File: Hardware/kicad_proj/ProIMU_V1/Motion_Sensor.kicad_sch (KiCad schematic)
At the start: 18 parts, among them U1 BMP280, U2 BNO055, Y1 Crystal

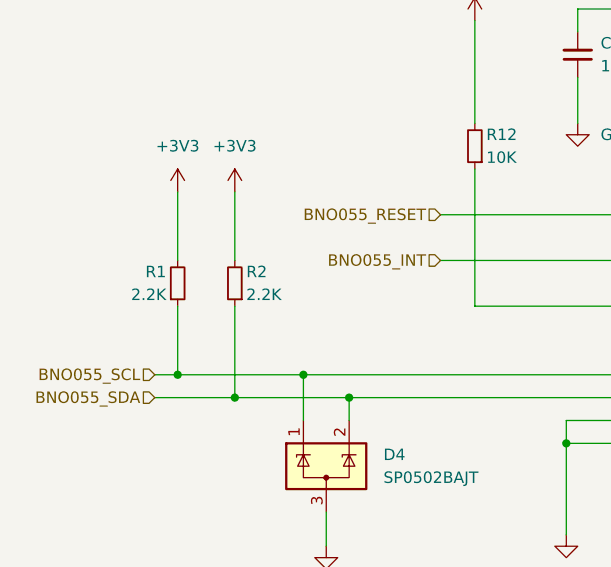
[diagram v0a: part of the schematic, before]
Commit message: Added New USB footprint. This will be used through entire project and will not be changed
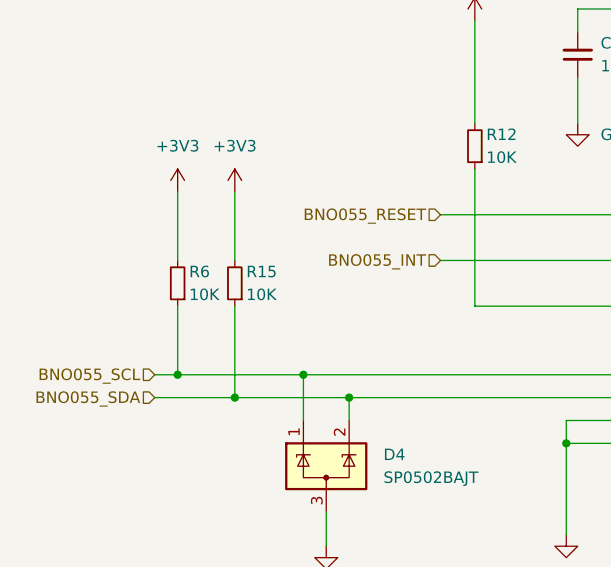
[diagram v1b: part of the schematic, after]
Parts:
- removed R1, R2: 2.2K, Resistor_SMD:R_0402_1005Metric_Pad0.72x0.64mm_HandSolder, symbol Device:R_Small
- added R15, R6: 10K, Resistor_SMD:R_0402_1005Metric_Pad0.72x0.64mm_HandSolder, symbol Device:R_Small
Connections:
- net +3V3: now also R15.2, R6.2
- net BNO055_SCL: now also R6.1
- net BNO055_SDA: now also R15.1
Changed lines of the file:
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@@
-    (pin "2")
-  )
-  (symbol (lib_id "Device:R_Small") (at 80.01 63.5 0) (mirror x) (unit 1)
-    (in_bom yes) (on_board yes)
-    (property "Reference" "R1" (id 0) (at 78.74 62.23 0)
-      (effects (font (size 1.27 1.27)) (justify right))
-    )
-    (property "Value" "2.2K" (id 1) (at 78.74 64.77 0)
-      (effects (font (size 1.27 1.27)) (justify right))
-    )
-    (property "Footprint" "Resistor_SMD:R_0402_1005Metric_Pad0.72x0.64mm_HandSolder" (id 2) (at 80.01 63.5 0)
-      (effects (font (size 1.27 1.27)) hide)
-    )
-    (property "Datasheet" "~" (id 3) (at 80.01 63.5 0)
-      (effects (font (size 1.27 1.27)) hide)
-    )
-    (pin "1")
     (pin "2")
   )
@@
     (pin "2")
   )
-  (symbol (lib_id "Device:R_Small") (at 86.36 63.5 180) (unit 1)
-    (in_bom yes) (on_board yes)
-    (property "Reference" "R2" (id 0) (at 87.63 62.23 0)
-      (effects (font (size 1.27 1.27)) (justify right))
-    )
-    (property "Value" "2.2K" (id 1) (at 87.63 64.77 0)
-      (effects (font (size 1.27 1.27)) (justify right))
-    )
-    (property "Footprint" "Resistor_SMD:R_0402_1005Metric_Pad0.72x0.64mm_HandSolder" (id 2) (at 86.36 63.5 0)
-      (effects (font (size 1.27 1.27)) hide)
-    )
-    (property "Datasheet" "~" (id 3) (at 86.36 63.5 0)
-      (effects (font (size 1.27 1.27)) hide)
-    )
-    (pin "1")
-    (pin "2")
-  )
   (symbol (lib_id "power:GND") (at 167.64 134.62 90) (unit 1)
     (in_bom yes) (on_board yes) (fields_autoplaced)
@@
     (pin "1")
   )
+  (symbol (lib_id "Device:R_Small") (at 86.36 63.5 180) (unit 1)
+    (in_bom yes) (on_board yes)
+    (property "Reference" "R15" (id 0) (at 87.63 62.23 0)
+      (effects (font (size 1.27 1.27)) (justify right))
+    )
+    (property "Value" "10K" (id 1) (at 87.63 64.77 0)
+      (effects (font (size 1.27 1.27)) (justify right))
+    )
+    (property "Footprint" "Resistor_SMD:R_0402_1005Metric_Pad0.72x0.64mm_HandSolder" (id 2) (at 86.36 63.5 0)
+      (effects (font (size 1.27 1.27)) hide)
+    )
+    (property "Datasheet" "~" (id 3) (at 86.36 63.5 0)
+      (effects (font (size 1.27 1.27)) hide)
+    )
+    (pin "1")
+    (pin "2")
+  )
   (symbol (lib_id "power:GND") (at 182.88 127 0) (unit 1)
     (in_bom yes) (on_board yes) (fields_autoplaced)
@@
       (effects (font (size 1.27 1.27)) hide)
     )
+    (pin "1")
+    (pin "2")
+  )
+  (symbol (lib_id "Device:R_Small") (at 80.01 63.5 180) (unit 1)
+    (in_bom yes) (on_board yes)
+    (property "Reference" "R6" (id 0) (at 81.28 62.23 0)
+      (effects (font (size 1.27 1.27)) (justify right))
+    )
+    (property "Value" "10K" (id 1) (at 81.28 64.77 0)
+      (effects (font (size 1.27 1.27)) (justify right))
+    )
+    (property "Footprint" "Resistor_SMD:R_0402_1005Metric_Pad0.72x0.64mm_HandSolder" (id 2) (at 80.01 63.5 0)
+      (effects (font (size 1.27 1.27)) hide)
+    )
+    (property "Datasheet" "~" (id 3) (at 80.01 63.5 0)
+      (effects (font (size 1.27 1.27)) hide)
+    )

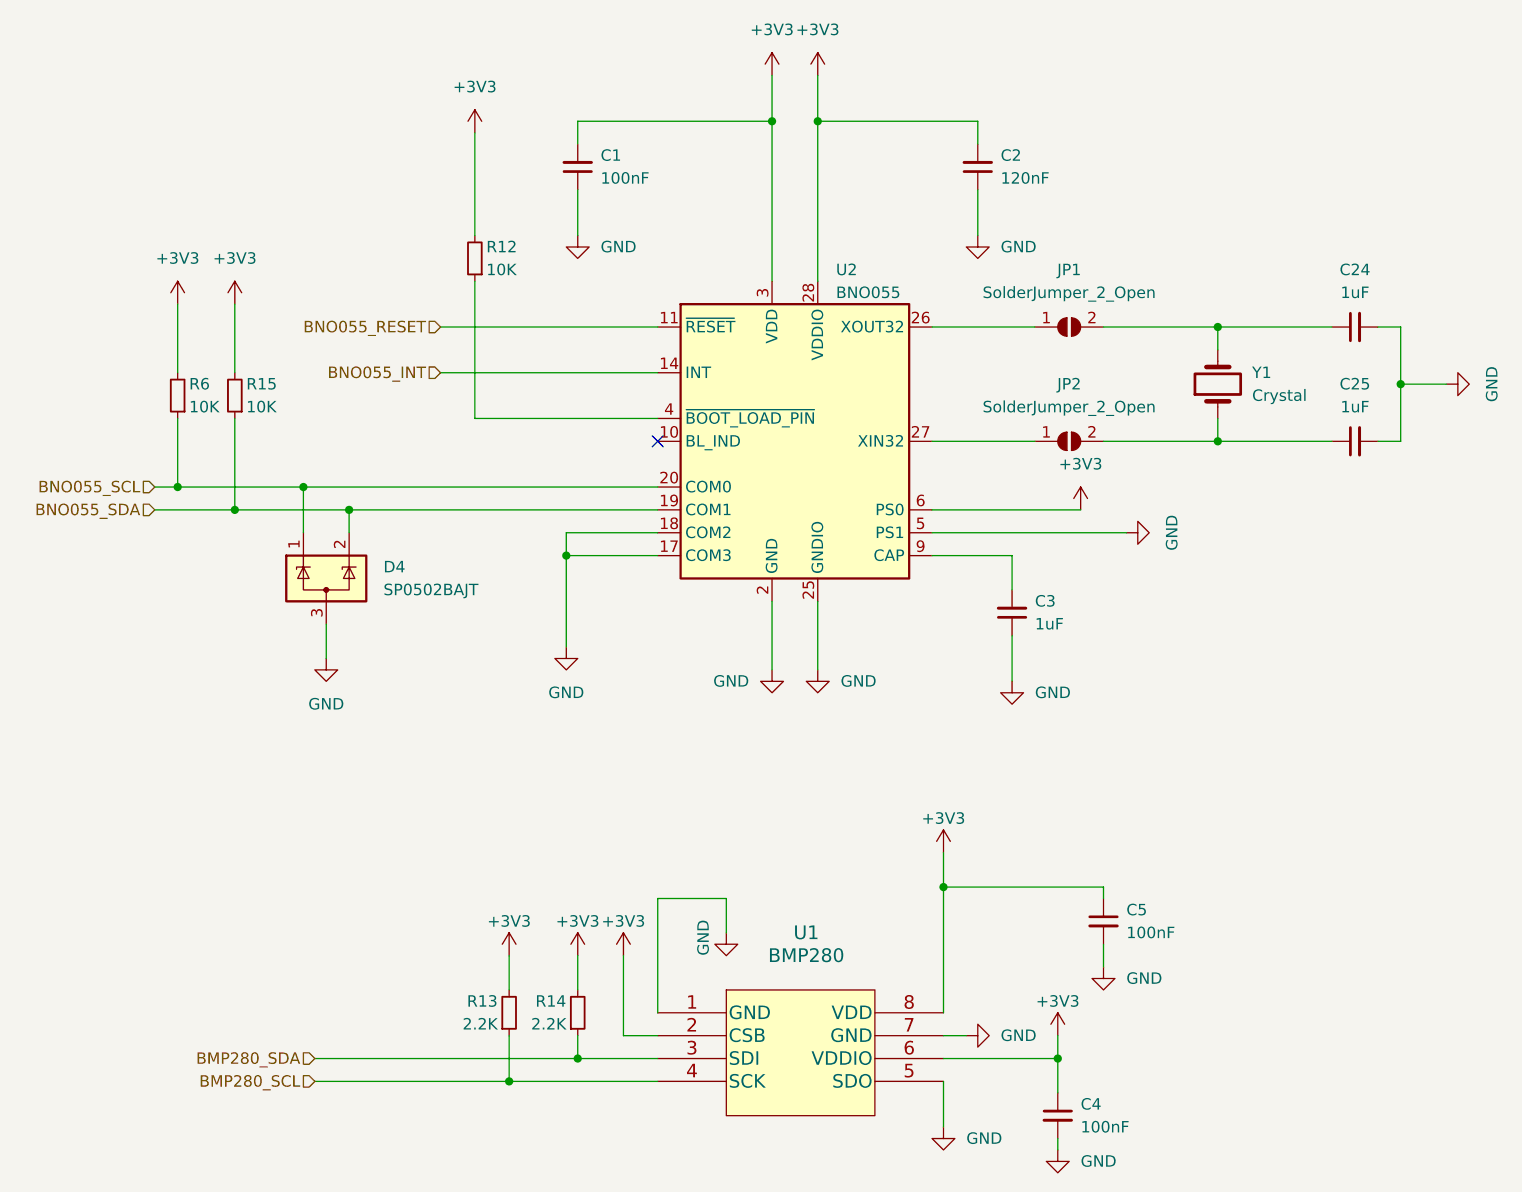
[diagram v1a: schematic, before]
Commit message: Updated schematic and layout
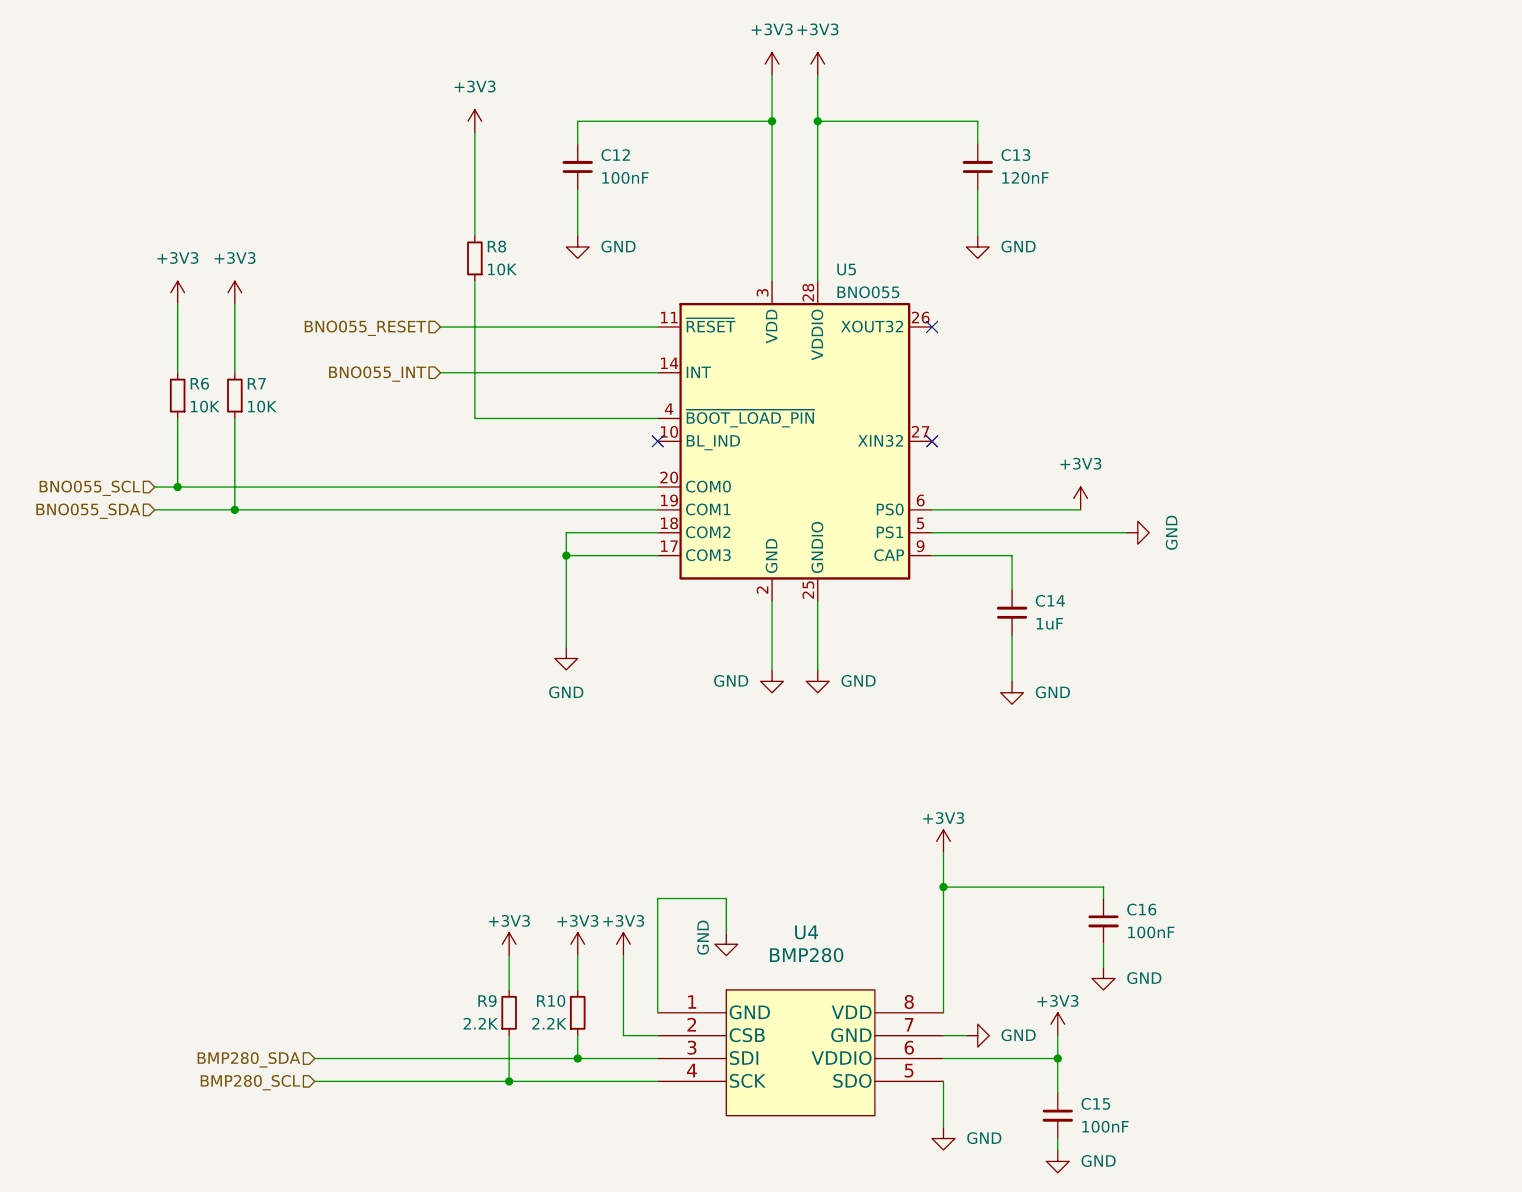
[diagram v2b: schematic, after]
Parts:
- removed C24, C25: 1uF, Capacitor_SMD:C_0402_1005Metric_Pad0.74x0.62mm_HandSolder, symbol Device:C_Small
- removed D4: SP0502BAJT, Package_TO_SOT_SMD:SOT-323_SC-70, symbol Power_Protection:SP0502BAJT
- removed JP1, JP2: SolderJumper_2_Open, Jumper:SolderJumper-2_P1.3mm_Open_RoundedPad1.0x1.5mm, symbol Jumper:SolderJumper_2_Open
- removed Y1: Crystal, Crystal:Crystal_SMD_3215-2Pin_3.2x1.5mm, symbol Device:Crystal
- renumbered C1 to C12, C2 to C13, C3 to C14, C4 to C15, C5 to C16, R14 to R10, R15 to R7, R12 to R8, R13 to R9, U1 to U4, U2 to U5
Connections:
- no-connect marks 1 -> 3
